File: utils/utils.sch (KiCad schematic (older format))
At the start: 22 parts, among them J6 EURORACK_CONN_16, Q1 2N3904, Q2 2N3904, Q3 2N3904, U1 TL074, U2 DG403

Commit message: rework PCB
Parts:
- R1, R3, R8: footprint Resistor_THT:R_Axial_DIN0309_L9.0mm_D3.2mm_P2.54mm_Vertical -> Resistor_THT:R_Axial_DIN0204_L3.6mm_D1.6mm_P5.08mm_Horizontal
- renumbered A_IN to A_IN1, B_IN to B_IN1
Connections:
- net CONST: now also U2.10 (IN2); no longer U2.15 (IN1)
- net GATE: now also U2.15 (IN1); no longer U2.10 (IN2)
- net GND: now also U2.3 (D3); no longer U2.6 (D4)
- net at R6.1, U1.12 (+): now also U2.16 (S1), U2.4 (S3); no longer U2.5 (S4), U2.9 (S2)
- net at RV1.4, U1.7: now also U2.6 (D4); no longer U2.3 (D3)
- net at U1.1, U1.2 (-): now also U2.8 (D2); no longer U2.1 (D1)
- new net: U2.1 (D1), U2.5 (S4), U2.9 (S2)
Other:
- moved on the sheet: U2A, U2B
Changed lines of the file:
@@
 F 0 "R8" H 7320 5846 50  0000 L CNN
 F 1 "1K" H 7320 5755 50  0000 L CNN
-F 2 "Resistor_THT:R_Axial_DIN0309_L9.0mm_D3.2mm_P2.54mm_Vertical" V 7180 5800 50  0001 C CNN
+F 2 "Resistor_THT:R_Axial_DIN0204_L3.6mm_D1.6mm_P5.08mm_Horizontal" V 7180 5800 50  0001 C CNN
 F 3 "~" H 7250 5800 50  0001 C CNN
 	1    7250 5800
@@
 F 0 "R3" V 3343 3450 50  0000 C CNN
 F 1 "100K" V 3434 3450 50  0000 C CNN
-F 2 "Resistor_THT:R_Axial_DIN0309_L9.0mm_D3.2mm_P2.54mm_Vertical" V 3480 3450 50  0001 C CNN
+F 2 "Resistor_THT:R_Axial_DIN0204_L3.6mm_D1.6mm_P5.08mm_Horizontal" V 3480 3450 50  0001 C CNN
 F 3 "~" H 3550 3450 50  0001 C CNN
 	1    3550 3450
@@
 L synth:DG403 U2
 U 1 1 5F0435F7
+P 6050 3050
+F 0 "U2" H 6050 3275 50  0000 C CNN
+F 1 "DG403" H 6050 3184 50  0000 C CNN
+F 2 "Package_SO:SOIC-16_3.9x9.9mm_P1.27mm" H 6050 2350 50  0001 C CNN
+F 3 "https://www.renesas.com/us/en/www/doc/datasheet/dg401-03.pdf" H 6050 3050 50  0001 C CNN
+	1    6050 3050
+	-1   0    0    -1
+$EndComp
+$Comp
+L synth:DG403 U2
+U 2 1 5F0A3698
 P 5250 2850
 F 0 "U2" H 5250 3075 50  0000 C CNN
@@
 F 2 "Package_SO:SOIC-16_3.9x9.9mm_P1.27mm" H 5250 2150 50  0001 C CNN
 F 3 "https://www.renesas.com/us/en/www/doc/datasheet/dg401-03.pdf" H 5250 2850 50  0001 C CNN
-	1    5250 2850
-	-1   0    0    -1
-$EndComp
-$Comp
-L synth:DG403 U2
-U 2 1 5F0A3698
-P 6050 3050
-F 0 "U2" H 6050 3275 50  0000 C CNN
-F 1 "DG403" H 6050 3184 50  0000 C CNN
-F 2 "Package_SO:SOIC-16_3.9x9.9mm_P1.27mm" H 6050 2350 50  0001 C CNN
-F 3 "https://www.renesas.com/us/en/www/doc/datasheet/dg401-03.pdf" H 6050 3050 50  0001 C CNN
-	2    6050 3050
+	2    5250 2850
 	-1   0    0    -1
 $EndComp
@@
 F 0 "R1" H 3070 6596 50  0000 L CNN
 F 1 "100K" H 3070 6505 50  0000 L CNN
-F 2 "Resistor_THT:R_Axial_DIN0309_L9.0mm_D3.2mm_P2.54mm_Vertical" V 2930 6550 50  0001 C CNN
+F 2 "Resistor_THT:R_Axial_DIN0204_L3.6mm_D1.6mm_P5.08mm_Horizontal" V 2930 6550 50  0001 C CNN
 F 3 "~" H 3000 6550 50  0001 C CNN
 	1    3000 6550
@@
 $EndComp
 $Comp
-L synth:AudioJack2_Ground_Switch B_IN
+L synth:AudioJack2_Ground_Switch B_IN1
 U 1 1 5F170E51
 P 1200 2350
-F 0 "B_IN" H 1232 2775 50  0000 C CNN
+F 0 "B_IN1" H 1232 2775 50  0000 C CNN
 F 1 "AudioJack2_Ground_Switch" H 1232 2684 50  0000 C CNN
 F 2 "synth:Jack_3.5mm_Ledino_KB3SPRS_Horizontal" H 1200 2550 50  0001 C CNN
@@
 $EndComp
 $Comp
-L synth:AudioJack2_Ground_Switch A_IN
+L synth:AudioJack2_Ground_Switch A_IN1
 U 1 1 5F14C66A
 P 1200 1200
-F 0 "A_IN" H 1232 1625 50  0000 C CNN
+F 0 "A_IN1" H 1232 1625 50  0000 C CNN
 F 1 "AudioJack2_Ground_Switch" H 1232 1534 50  0000 C CNN
 F 2 "synth:Jack_3.5mm_Ledino_KB3SPRS_Horizontal" H 1200 1400 50  0001 C CNN

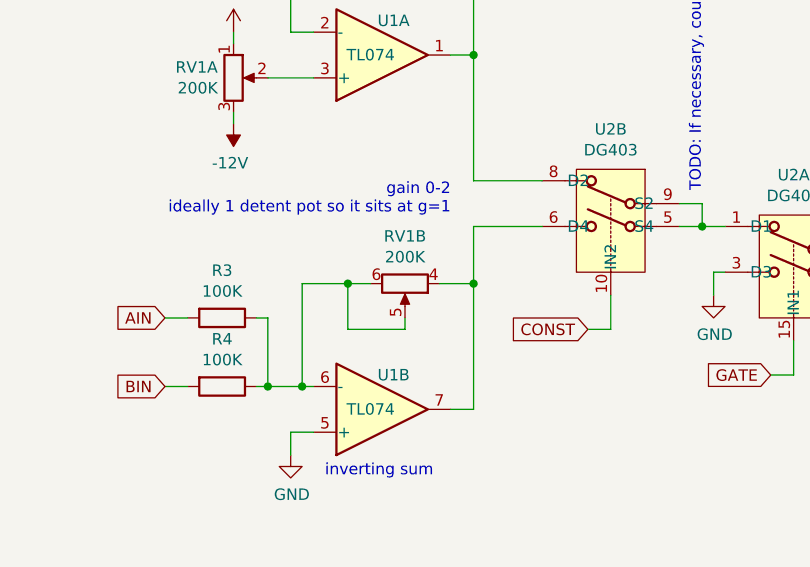
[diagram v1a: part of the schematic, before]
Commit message: corrected pin order on the pot breakout
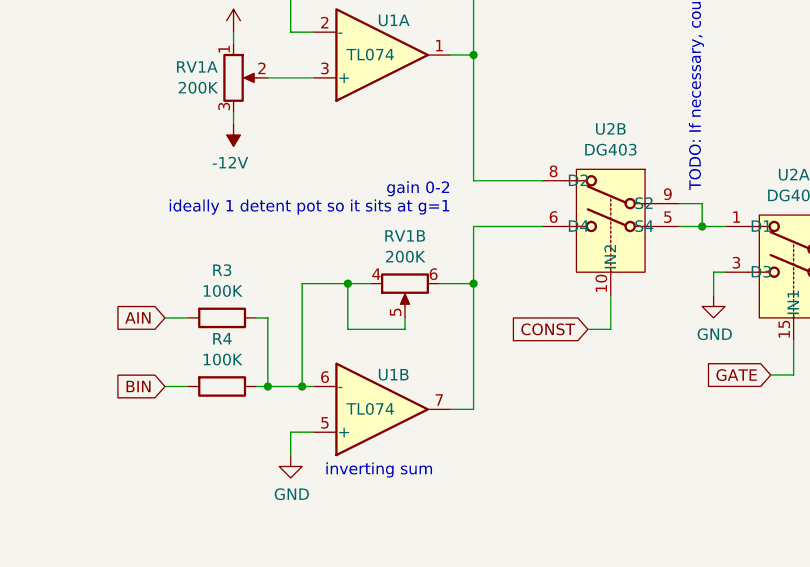
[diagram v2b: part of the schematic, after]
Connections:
- net at R3.1, R4.1, RV1.5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: now also RV1.4; no longer RV1.6
- net at U1.7, U2.6 (D4): now also RV1.6; no longer RV1.4
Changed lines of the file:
@@
 F 3 "~" H 4350 3300 50  0001 C CNN
 	2    4350 3300
-	0    1    1    0
+	0    -1   1    0
 $EndComp
 $Comp

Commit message: cleanup
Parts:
- R1, R3, R8: footprint Resistor_THT:R_Axial_DIN0204_L3.6mm_D1.6mm_P5.08mm_Horizontal -> Resistor_THT:R_Axial_DIN0309_L9.0mm_D3.2mm_P2.54mm_Vertical
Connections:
- net at R3.1, R4.1, RV1.5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: now also RV1.6; no longer RV1.4
- net at U1.7, U2.6 (D4): now also RV1.4; no longer RV1.6
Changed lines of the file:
@@
 F 0 "R8" H 7320 5846 50  0000 L CNN
 F 1 "1K" H 7320 5755 50  0000 L CNN
-F 2 "Resistor_THT:R_Axial_DIN0204_L3.6mm_D1.6mm_P5.08mm_Horizontal" V 7180 5800 50  0001 C CNN
+F 2 "Resistor_THT:R_Axial_DIN0309_L9.0mm_D3.2mm_P2.54mm_Vertical" V 7180 5800 50  0001 C CNN
 F 3 "~" H 7250 5800 50  0001 C CNN
 	1    7250 5800
@@
 F 3 "~" H 4350 3300 50  0001 C CNN
 	2    4350 3300
-	0    -1   1    0
+	0    1    1    0
 $EndComp
 $Comp
@@
 F 0 "R3" V 3343 3450 50  0000 C CNN
 F 1 "100K" V 3434 3450 50  0000 C CNN
-F 2 "Resistor_THT:R_Axial_DIN0204_L3.6mm_D1.6mm_P5.08mm_Horizontal" V 3480 3450 50  0001 C CNN
+F 2 "Resistor_THT:R_Axial_DIN0309_L9.0mm_D3.2mm_P2.54mm_Vertical" V 3480 3450 50  0001 C CNN
 F 3 "~" H 3550 3450 50  0001 C CNN
 	1    3550 3450
@@
 F 0 "R1" H 3070 6596 50  0000 L CNN
 F 1 "100K" H 3070 6505 50  0000 L CNN
-F 2 "Resistor_THT:R_Axial_DIN0204_L3.6mm_D1.6mm_P5.08mm_Horizontal" V 2930 6550 50  0001 C CNN
+F 2 "Resistor_THT:R_Axial_DIN0309_L9.0mm_D3.2mm_P2.54mm_Vertical" V 2930 6550 50  0001 C CNN
 F 3 "~" H 3000 6550 50  0001 C CNN
 	1    3000 6550

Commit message: tested utils rev b
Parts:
- R8: value 1K -> 10K
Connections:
- net +12V: now also D1.2 (A), R1.1, R5.1
- net +5V: no longer D1.2 (A), R1.1, R5.1
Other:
- note added: "TODO from sample:\nsumming pot is backwards\nnoise near center of constant\nhard click on gate"
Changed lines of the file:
@@
 P 7250 5800
 F 0 "R8" H 7320 5846 50  0000 L CNN
-F 1 "1K" H 7320 5755 50  0000 L CNN
+F 1 "10K" H 7320 5755 50  0000 L CNN
 F 2 "Resistor_THT:R_Axial_DIN0309_L9.0mm_D3.2mm_P2.54mm_Vertical" V 7180 5800 50  0001 C CNN
 F 3 "~" H 7250 5800 50  0001 C CNN
@@
 Wire Wire Line
 	7250 5050 7250 5150
-Wire Wire Line
-	7250 4650 7250 4750
 Wire Wire Line
 	6700 4800 6800 4800
@@
 	4000 6850 4100 6850
 $Comp
-L Device:R R1
-U 1 1 5F30ADA8
-P 3000 6550
-F 0 "R1" H 3070 6596 50  0000 L CNN
-F 1 "100K" H 3070 6505 50  0000 L CNN
-F 2 "Resistor_THT:R_Axial_DIN0309_L9.0mm_D3.2mm_P2.54mm_Vertical" V 2930 6550 50  0001 C CNN
-F 3 "~" H 3000 6550 50  0001 C CNN
-	1    3000 6550
-	1    0    0    -1
-$EndComp
-$Comp
 L Device:R R2
 U 1 1 5F30B3D5
@@
 F 3 "~" H 3400 5750 50  0001 C CNN
 	1    3400 5750
-	1    0    0    -1
-$EndComp
-$Comp
-L Device:R R5
-U 1 1 5F30B999
-P 4000 6600
-F 0 "R5" H 4070 6646 50  0000 L CNN
-F 1 "100K" H 4070 6555 50  0000 L CNN
-F 2 "Resistor_THT:R_Axial_DIN0309_L9.0mm_D3.2mm_P2.54mm_Vertical" V 3930 6600 50  0001 C CNN
-F 3 "~" H 4000 6600 50  0001 C CNN
-	1    4000 6600
 	1    0    0    -1
 $EndComp
@@
 Wire Wire Line
 	1650 3000 1650 3550
-$Comp
-L power:+5V #PWR017
-U 1 1 5F35A407
-P 7250 4650
-F 0 "#PWR017" H 7250 4500 50  0001 C CNN
-F 1 "+5V" H 7265 4823 50  0000 C CNN
-F 2 "" H 7250 4650 50  0001 C CNN
-F 3 "" H 7250 4650 50  0001 C CNN
-	1    7250 4650
-	1    0    0    -1
-$EndComp
 Wire Wire Line
 	3000 6850 3000 6700
@@
 	4000 6750 4000 6850
 Connection ~ 4000 6850
-$Comp
-L power:+5V #PWR07
-U 1 1 5F3963B4
-P 3000 6300
-F 0 "#PWR07" H 3000 6150 50  0001 C CNN
-F 1 "+5V" H 3015 6473 50  0000 C CNN
-F 2 "" H 3000 6300 50  0001 C CNN
-F 3 "" H 3000 6300 50  0001 C CNN
-	1    3000 6300
-	1    0    0    -1
-$EndComp
 Wire Wire Line
 	3000 6300 3000 6400
-$Comp
-L power:+5V #PWR013
-U 1 1 5F39D487
-P 4000 6300
-F 0 "#PWR013" H 4000 6150 50  0001 C CNN
-F 1 "+5V" H 4015 6473 50  0000 C CNN
-F 2 "" H 4000 6300 50  0001 C CNN
-F 3 "" H 4000 6300 50  0001 C CNN
-	1    4000 6300
-	1    0    0    -1
-$EndComp
 Wire Wire Line
 	4000 6300 4000 6450
@@
 	6800 5550 6800 5350
 Connection ~ 6800 5350
-Text Notes 5650 2900 1    50   ~ 0
-TODO: If necessary, could move the buffer of ~OUT~ to here
 Wire Wire Line
 	5700 3350 5700 3250
@@
 	1    0    0    -1
 $EndComp
+$Comp
+L Device:R R1
+U 1 1 5F30ADA8
+P 3000 6550
+F 0 "R1" H 3070 6596 50  0000 L CNN
+F 1 "100K" H 3070 6505 50  0000 L CNN
+F 2 "Resistor_THT:R_Axial_DIN0309_L9.0mm_D3.2mm_P2.54mm_Vertical" V 2930 6550 50  0001 C CNN
+F 3 "~" H 3000 6550 50  0001 C CNN
+	1    3000 6550
+	1    0    0    -1
+$EndComp
+$Comp
+L Device:R R5
+U 1 1 5F30B999
+P 4000 6600
+F 0 "R5" H 4070 6646 50  0000 L CNN
+F 1 "100K" H 4070 6555 50  0000 L CNN
+F 2 "Resistor_THT:R_Axial_DIN0309_L9.0mm_D3.2mm_P2.54mm_Vertical" V 3930 6600 50  0001 C CNN
+F 3 "~" H 4000 6600 50  0001 C CNN
+	1    4000 6600
+	1    0    0    -1
+$EndComp
+Wire Wire Line
+	7250 4650 7250 4750
+$Comp
+L power:+12V #PWR?
+U 1 1 5F168A18
+P 7250 4650
+F 0 "#PWR?" H 7250 4500 50  0001 C CNN
+F 1 "+12V" H 7265 4823 50  0000 C CNN
+F 2 "" H 7250 4650 50  0001 C CNN
+F 3 "" H 7250 4650 50  0001 C CNN
+	1    7250 4650
+	1    0    0    -1
+$EndComp
+$Comp
+L power:+12V #PWR?
+U 1 1 5F168FE2
+P 4000 6300
+F 0 "#PWR?" H 4000 6150 50  0001 C CNN
+F 1 "+12V" H 4015 6473 50  0000 C CNN
+F 2 "" H 4000 6300 50  0001 C CNN
+F 3 "" H 4000 6300 50  0001 C CNN
+	1    4000 6300
+	1    0    0    -1
+$EndComp
+$Comp
+L power:+12V #PWR?
+U 1 1 5F16998A
+P 3000 6300
+F 0 "#PWR?" H 3000 6150 50  0001 C CNN
+F 1 "+12V" H 3015 6473 50  0000 C CNN
+F 2 "" H 3000 6300 50  0001 C CNN
+F 3 "" H 3000 6300 50  0001 C CNN
+	1    3000 6300
+	1    0    0    -1
+$EndComp
+Text Notes 8750 3600 0    50   ~ 0
+TODO from sample:\nsumming pot is backwards\nnoise near center of constant\nhard click on gate
+Text Notes 5650 2900 1    50   ~ 0
+TODO: If necessary, could move the buffer of ~OUT~ to here
 $EndSCHEMATC

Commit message: util tweaks
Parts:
- removed J6: EURORACK_CONN_16, synth:EURORACK_16_IDC, symbol synth:EURORACK_CONN_16
- added D?: D, symbol Device:D
- added J1: EURORACK_CONN_10, synth:EURORACK_10_IDC, symbol synth:EURORACK_CONN_10
- added R? (x2): 130K, Resistor_THT:R_Axial_DIN0309_L9.0mm_D3.2mm_P2.54mm_Vertical, symbol Device:R
- added R?: 100K, Resistor_THT:R_Axial_DIN0309_L9.0mm_D3.2mm_P2.54mm_Vertical, symbol Device:R
- added SW? (x2): SW_BI_UNI, symbol Switch:SW_DPDT_x2
- added SW?: SW_BI_UNI, symbol Switch:SW_Push
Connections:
- net +5V is gone; now on net +12V: GATE1.TN, R2.1, U2.12 (VL)
- net +12V: now also J1.9 (12V_P), R?.2, R?.2; no longer RV1.1
- net -12V: now also J1.1 (12V_N), R?.1, SW?.3 (C); no longer RV1.3
- net GATE: now also Q3.2 (B), SW?.1
- net GND: now also GATE1.SN, R7.2, J1.3 (GND), SW?.1 (A), SW?.4 (A); no longer U2.3 (D3)
- net at R8.1: now also D?.1 (K); no longer Q3.1 (E)
- removed net GATE_CONN: GATE1.SN, Q3.2 (B), R7.2
- new net: D?.2 (A), Q3.1 (E)
- new net: R?.1, RV1.1
- new net: RV1.3, SW?.5 (B)
- new net: SW?.2 (B), U2.3 (D3)
- new net: R?.2, SW?.6 (C)
- new net: R?.1, SW?.2
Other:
- note added: "-5v to +5v constant"
- note added: "TODO diode is to put the level the gate turns on the led\ncloser to the one of the switch (~2.4V)"
- note added: "When either AIN or BIN is connected, the ground\nat *_CONN is disconnected, turning the transistor\non, shorting control of the first switch low, which\nswitches from the constant voltage source to the\nsumming source"
- note added: "center detent pot so it sits at g=1"
- note removed: "TODO: If necessary, could move the buffer of ~OUT~ to here"
- note removed: "This is a trick to only use the LED to show gate state\nif the GATE jack is used. When jack is unplugged,\nGATE_CONN is grounded, turning off the transistor.\nWhen jack is plugged, GATE_CONN floats, allowing\nthe gate to control the transistor. R10 gives an input\nimpedance of 100K, since LED is driven by power\nsupply. LED on current depends on GATE"
- note removed: "When either AIN or BIN is connected, the ground\nat *_CONN is disconnected, turining the transistor\non, shorting control of the first switch low, which\nswitches from the constant voltage source to the\nsumming source"
- note removed: "gain 0-2\nideally 1 detent pot so it sits at g=1"
- moved on the sheet: D1, Q3, R6, R7, R8, R9, RV1A, U1A, U1C, U1D, U2A
